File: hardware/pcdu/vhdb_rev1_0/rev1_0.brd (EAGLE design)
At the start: 100 x 35 mm, 64 parts, among them J1 AJP92A8813, J2 AJP92A8813, J3 AJP92A8813, J4 AJP92A8813, J5 AJP92A8813, Q1 25MHz, SW1 KSZ9897RTXC

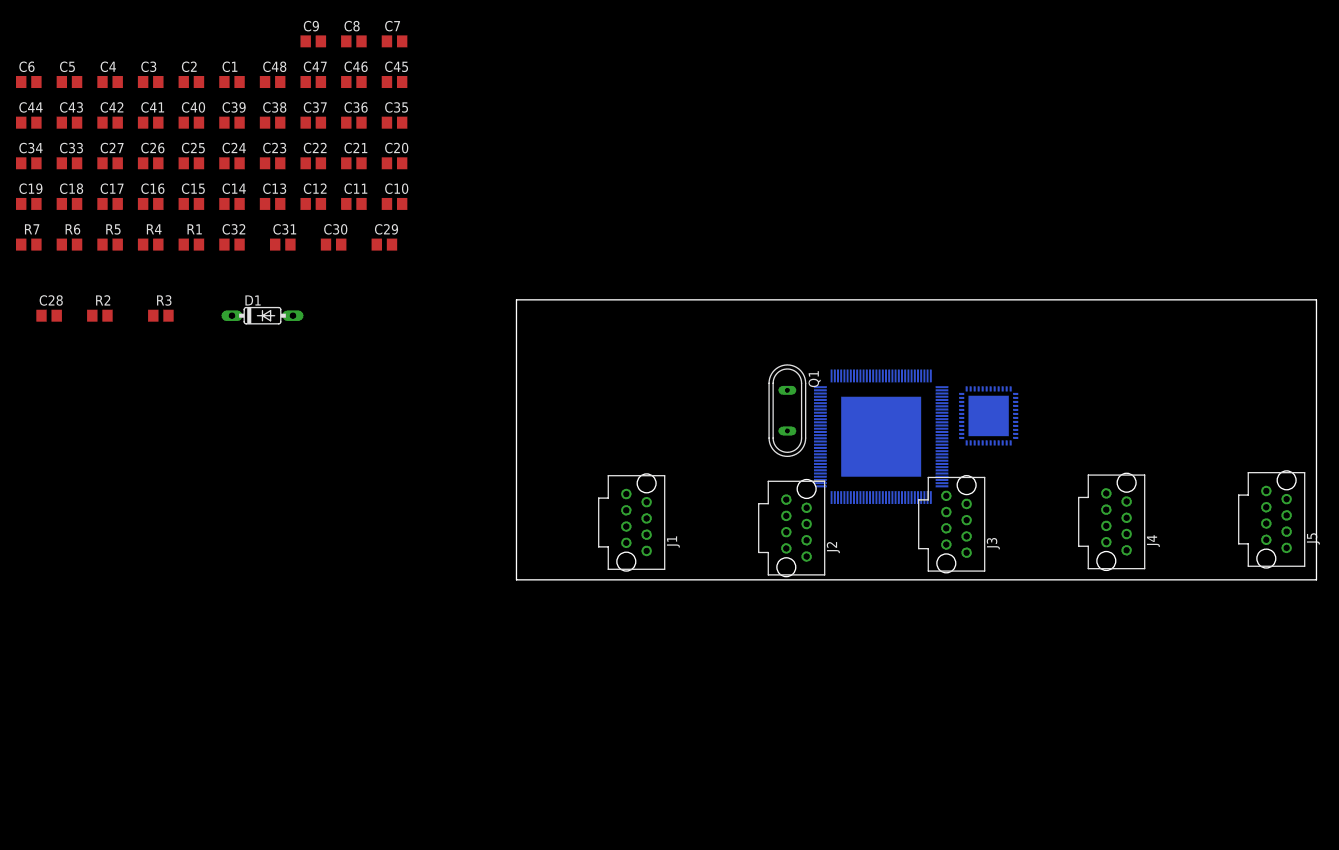
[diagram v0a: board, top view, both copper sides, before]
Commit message: Added lan transformers
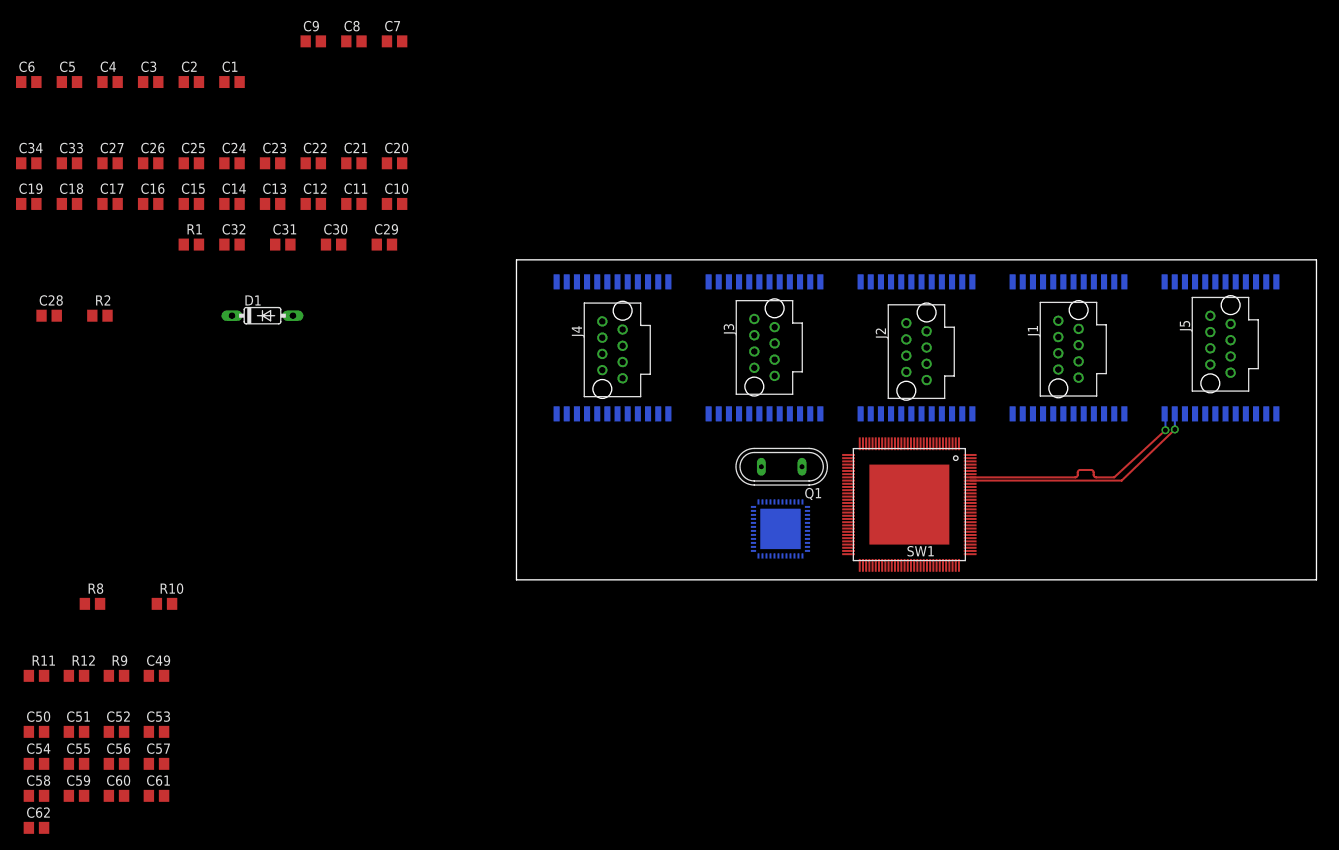
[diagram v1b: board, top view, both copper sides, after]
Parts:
- removed C35, C36, C37, C38, C39, C40, C41, C42, C43, C44, C45, C46, C47, C48: (no value), rcl:C0805
- removed PHY1: KSZ9031RNX, KSZ9031RNX:KSZ9031RNX
- removed R3: 12.1 kΩ, resistor:R0805
- removed R4, R5, R6, R7: 10K, resistor:R0805
- added C49, C50, C51, C52, C53, C54, C55, C56, C57, C58, C59, C60, C61, C62: (no value), rcl:C0805
- added MAG1, MAG2, MAG3, MAG4, MAG5: 749020010A, 749023010A:749023010A
- added PHY2: KSZ9031RNX, KSZ9031RNX:KSZ9031RNX
- added R10, R11, R12, R9: 10K, resistor:R0805
- added R8: 12.1 kΩ, resistor:R0805
- moved J4 66.6 mm to (12.0, 28.8), turned to 270 degrees
- moved J1 58.2 mm to (69.0, 28.8), turned to 270 degrees
- moved J3 32.6 mm to (31.0, 29.1), turned to 270 degrees
- moved J2 26.7 mm to (50.0, 28.5), turned to 270 degrees
- moved J5 23.0 mm to (88.0, 29.4), turned to 270 degrees
- moved SW1 9.18 mm to (49.1, 9.41), flipped to the top, turned to 180 degrees
- moved Q1 7.05 mm to (33.1, 14.1), turned to 180 degrees
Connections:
- removed net N$10: PHY1.TX_EN, SW1.TX_EN7/TX_CTL7
- removed net N$11: PHY1.GTX_CLK, SW1.TX_CLK7/REFCLKI7
- removed net N$12: PHY1.RX_DV/CLK125_EN, SW1.RX_DV7/CRS_DV7/RX_CTL7
- removed net N$13: PHY1.RX_CLK/PHYAD2, SW1.RX_CLK7/REFCLKO7
- removed net N$15: PHY1.ISET, R3.2
- removed net N$6: PHY1.TXD0, SW1.RXD7_0
- removed net N$7: PHY1.TXD1, SW1.RXD7_1
- removed net N$8: PHY1.TXD2, SW1.RXD7_2
- removed net N$9: PHY1.TXD3, SW1.RXD7_3
- new net D54_N: MAG5.TD4-, SW1.TXRX5M_D
- new net D54_P: MAG5.TD4+, SW1.TXRX5P_D
- new net N$1: MAG1.TD1+, SW1.TXRX1P_A
- new net N$100: PHY2.ISET, R8.2
- new net N$16: MAG1.TD3+, SW1.TXRX1P_C
- new net N$17: MAG1.TD3-, SW1.TXRX1M_C
- new net N$18: MAG1.TD4+, SW1.TXRX1P_D
- new net N$19: MAG1.TD4-, SW1.TXRX1M_D
- new net N$20: MAG2.TD1+, SW1.TXRX2P_A
- new net N$21: MAG2.TD1-, SW1.TXRX2M_A
- new net N$22: MAG2.TD2+, SW1.TXRX2P_B
- new net N$23: MAG2.TD2-, SW1.TXRX2M_B
- new net N$24: MAG2.TD3+, SW1.TXRX2P_C
- new net N$25: MAG2.TD3-, SW1.TXRX2M_C
- new net N$26: MAG2.TD4+, SW1.TXRX2P_D
- new net N$27: MAG2.TD4-, SW1.TXRX2M_D
- new net N$28: MAG3.TD1+, SW1.TXRX3P_A
- new net N$29: MAG3.TD1-, SW1.TXRX3M_A
- new net N$3: MAG1.TD1-, SW1.TXRX1M_A
- new net N$30: MAG3.TD2+, SW1.TXRX3P_B
- new net N$31: MAG3.TD2-, SW1.TXRX3M_B
- new net N$32: MAG3.TD3+, SW1.TXRX3P_C
- new net N$33: MAG3.TD3-, SW1.TXRX3M_C
- new net N$34: MAG3.TD4+, SW1.TXRX3P_D
- new net N$35: MAG3.TD4-, SW1.TXRX3M_D
- new net N$38: MAG5.TD3-, SW1.TXRX5M_C
- new net N$39: MAG5.TD3+, SW1.TXRX5P_C
- new net N$4: MAG1.TD2+, SW1.TXRX1P_B
- new net N$40: MAG5.TD2-, SW1.TXRX5M_B
- new net N$41: MAG5.TD2+, SW1.TXRX5P_B
- new net N$42: MAG5.TD1-, SW1.TXRX5M_A
- new net N$43: MAG5.TD1+, SW1.TXRX5P_A
- new net N$44: MAG4.TD4-, SW1.TXRX4M_D
- new net N$45: MAG4.TD4+, SW1.TXRX4P_D
- new net N$46: MAG4.TD3-, SW1.TXRX4M_C
- new net N$47: MAG4.TD3+, SW1.TXRX4P_C
- new net N$48: MAG4.TD2-, SW1.TXRX4M_B
- new net N$49: MAG4.TD2+, SW1.TXRX4P_B
- new net N$5: MAG1.TD2-, SW1.TXRX1M_B
- new net N$50: MAG4.TD1-, SW1.TXRX4M_A
- new net N$51: MAG4.TD1+, SW1.TXRX4P_A
- new net N$52: J1.A+, MAG1.MX1+
- new net N$53: J1.A-, MAG1.MX1-
- new net N$54: J1.B+, MAG1.MX2+
- new net N$55: J1.B-, MAG1.MX2-
- new net N$56: J1.C+, MAG1.MX3+
- new net N$57: J1.C-, MAG1.MX3-
- new net N$58: J1.D+, MAG1.MX4+
- new net N$59: J1.D-, MAG1.MX4-
- new net N$60: J2.A+, MAG2.MX1+
- new net N$61: J2.A-, MAG2.MX1-
- new net N$62: J2.B+, MAG2.MX2+
- new net N$63: J2.B-, MAG2.MX2-
- new net N$64: J2.C+, MAG2.MX3+
- new net N$65: J2.C-, MAG2.MX3-
- new net N$66: J2.D+, MAG2.MX4+
- new net N$67: J2.D-, MAG2.MX4-
- new net N$68: J3.A+, MAG3.MX1+
- new net N$69: J3.A-, MAG3.MX1-
- new net N$70: J3.B+, MAG3.MX2+
- new net N$71: J3.B-, MAG3.MX2-
- new net N$72: J3.C+, MAG3.MX3+
- new net N$73: J3.C-, MAG3.MX3-
- new net N$74: J3.D+, MAG3.MX4+
- new net N$75: J3.D-, MAG3.MX4-
- new net N$76: J4.A+, MAG4.MX1+
- new net N$77: J4.A-, MAG4.MX1-
- new net N$78: J4.B+, MAG4.MX2+
- new net N$79: J4.B-, MAG4.MX2-
- new net N$80: J4.C+, MAG4.MX3+
- new net N$81: J4.C-, MAG4.MX3-
- new net N$82: J4.D+, MAG4.MX4+
- new net N$83: J4.D-, MAG4.MX4-
- new net N$84: J5.A+, MAG5.MX1+
- new net N$85: J5.A-, MAG5.MX1-
- new net N$86: J5.B+, MAG5.MX2+
- new net N$87: J5.B-, MAG5.MX2-
- new net N$88: J5.C+, MAG5.MX3+
- new net N$89: J5.C-, MAG5.MX3-
- new net N$90: J5.D+, MAG5.MX4+
- new net N$91: J5.D-, MAG5.MX4-
- new net N$92: PHY2.TXD0, SW1.RXD6_0
- new net N$93: PHY2.TXD1, SW1.RXD6_1
- new net N$94: PHY2.TXD2, SW1.RXD6_2
- new net N$95: PHY2.TXD3, SW1.RXD6_3
- new net N$96: PHY2.RX_DV/CLK125_EN, SW1.RX_DV6/CRS_DV6/RX_CTL6
- new net N$97: PHY2.RX_CLK/PHYAD2, SW1.RX_CLK6/REFCLKO6
- new net N$98: PHY2.TX_EN, SW1.TX_EN6/TX_CTL6
- new net N$99: PHY2.GTX_CLK, SW1.TX_CLK6/REFCLKI6
- net AVDDH: now also PHY2.AVDDH@1, PHY2.AVDDH@2; no longer PHY1.AVDDH@1, PHY1.AVDDH@2
- net AVDDL: now also PHY2.AVDDL@1, PHY2.AVDDL@2, PHY2.AVDDL_PLL; no longer PHY1.AVDDL@1, PHY1.AVDDL@2, PHY1.AVDDL_PLL
- net DVDDL: now also C49.1, PHY2.DVDDL@1, PHY2.DVDDL@2, PHY2.DVDDL@3, PHY2.DVDDL@4, PHY2.DVDDL@5, PHY2.DVDDL@6; no longer C35.1, PHY1.DVDDL@1, PHY1.DVDDL@2, PHY1.DVDDL@3, PHY1.DVDDL@4, PHY1.DVDDL@5, PHY1.DVDDL@6
- net GND: now also C49.2, C51.2, C52.2, C53.2, C54.2, C55.2, C57.2, C58.2, C60.2, C61.2, C62.2, PHY2.P_GND, PHY2.VSS, R12.1, R8.1; no longer C35.2, C37.2, C38.2, C39.2, C40.2, C41.2, C43.2, C44.2, C46.2, C47.2, C48.2, PHY1.P_GND, PHY1.VSS, R3.1, R7.1
- net MODE0: now also PHY2.RXD0/MODE0, R12.2, SW1.TXD6_0; no longer PHY1.RXD0/MODE0, R7.2, SW1.TXD7_0
- net MODE1: now also PHY2.RXD1/MODE1, R11.2, SW1.TXD6_1; no longer PHY1.RXD1/MODE1, R6.2
- net MODE2: now also PHY2.RXD2/MODE2, R10.2, SW1.TXD6_2; no longer PHY1.RXD2/MODE2, R5.2
- net MODE3: now also PHY2.RXD3/MODE3, R9.2, SW1.TXD6_3; no longer PHY1.RXD3/MODE3, R4.2, SW1.TXD7_3
- net RESET: now also PHY2.RESET_N; no longer PHY1.RESET_N
- net VDDIO: now also PHY2.DVDDH@1, PHY2.DVDDH@2, PHY2.DVDDH@3, R10.1, R11.1, R9.1; no longer PHY1.DVDDH@1, PHY1.DVDDH@2, PHY1.DVDDH@3, R4.1, R5.1, R6.1
- net XI: now also PHY2.XI; no longer PHY1.XI
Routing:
- net D54_P: track 0.00 -> 30.1 mm, vias 0 -> 1
- net D54_N: track 0.00 -> 29.9 mm, vias 0 -> 1
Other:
- board size 100 x 35 mm -> 100 x 40 mm
